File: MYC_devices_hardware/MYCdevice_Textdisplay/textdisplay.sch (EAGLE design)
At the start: 25 parts, among them IC1 MEGA8-P, IC2 78L05, Q1 20MHz, Q2 BC307, X1 8-15V, X2 1503_09, X3 1503_09

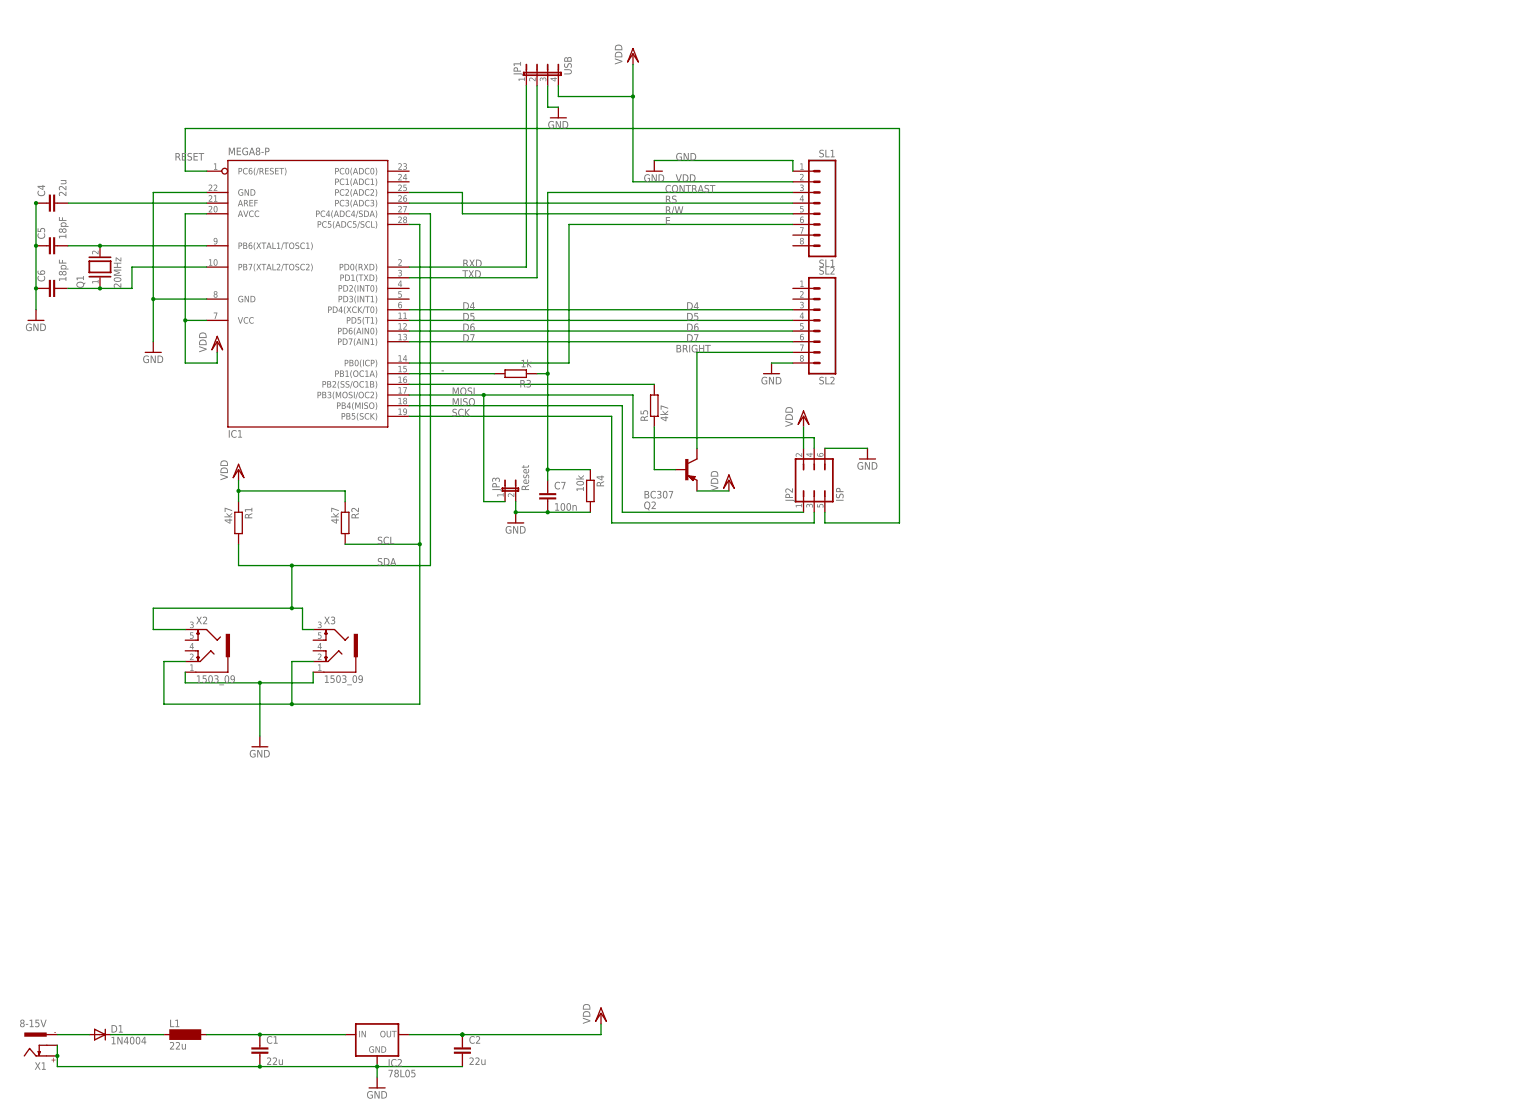
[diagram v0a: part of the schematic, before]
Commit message: now with includefiles, new board
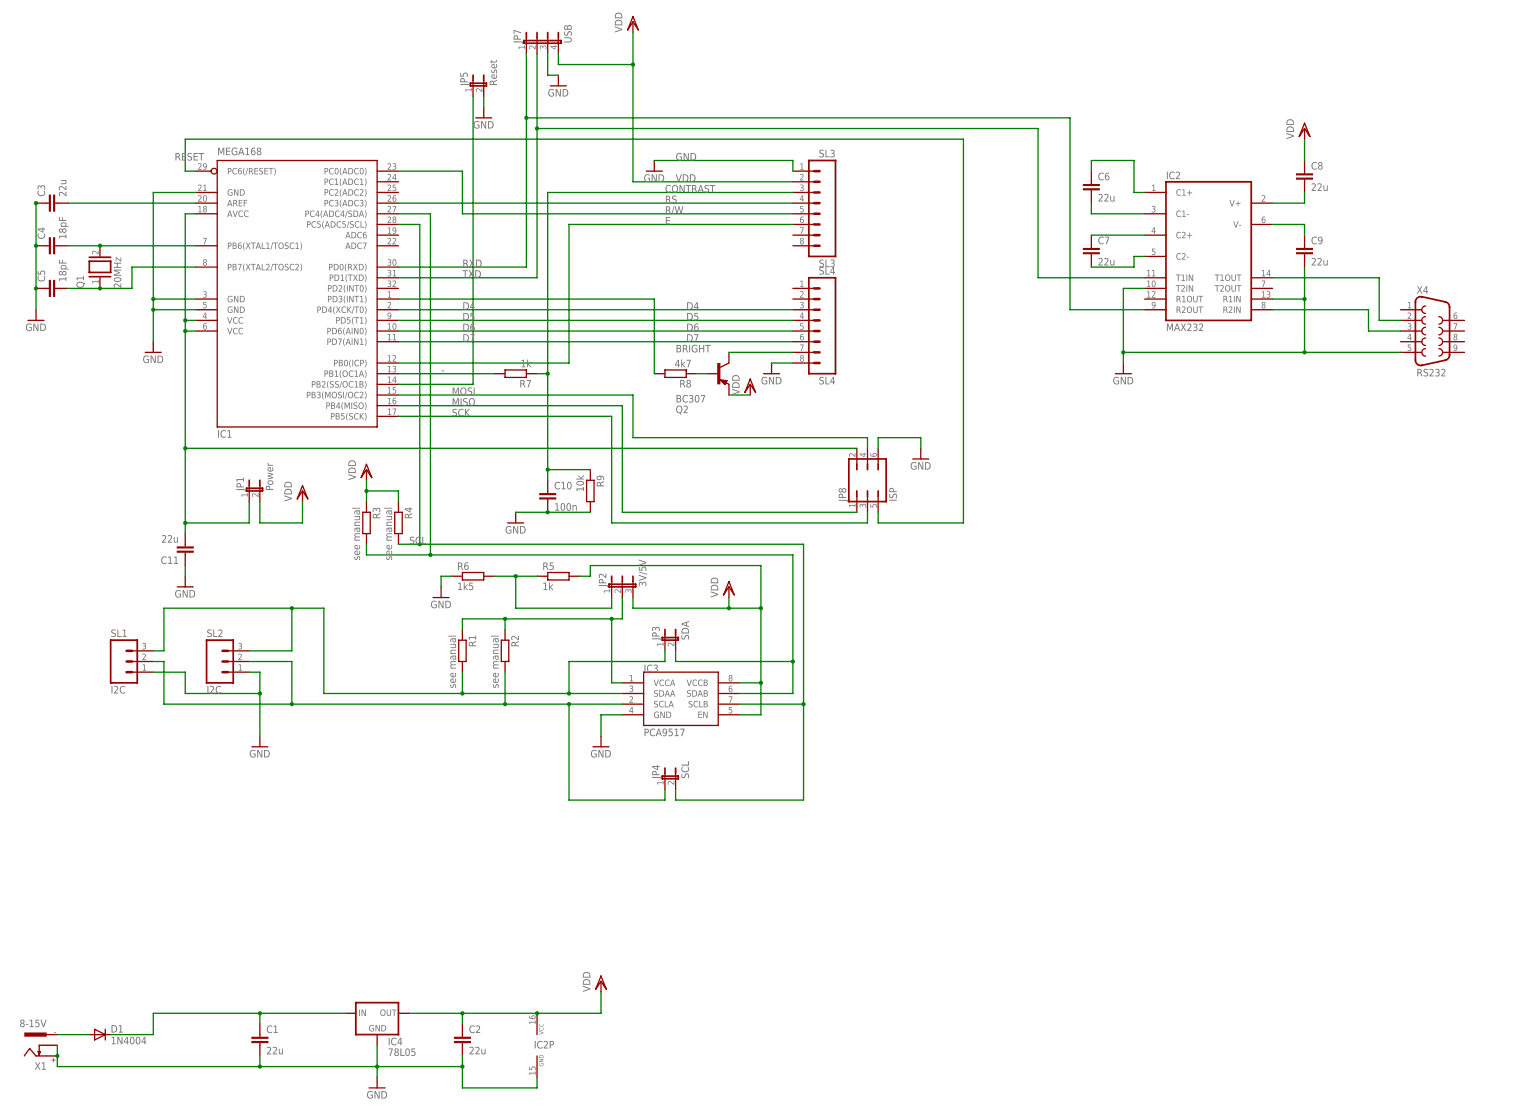
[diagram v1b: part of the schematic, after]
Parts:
- removed L1: 22u, inductor-neosid:MS85
- removed X2, X3: 1503_09, con-lumberg:1503_09
- added C10: 100n, resistor:C-EU050-025X075
- added C11, C3, C8, C9: 22u, resistor:C-EUC1206
- added IC3: PCA9517, PCA9517:PCA9517
- added IC4: 78L05, v-reg:78LXX
- added JP4: SCL, jumper:JP1E
- added JP5: Reset, jumper:JP1E
- added JP7: USB, jumper:JP4E
- added JP8: ISP, jumper:JP3Q
- added R6: 1k5, resistor:R-EU_R1206
- added R7: 1k, resistor:R-EU_R1206
- added R8: 4k7, resistor:R-EU_R1206
- added R9: 10k, resistor:R-EU_R1206
- added SL3: SL3, con-amp-quick:M08
- added SL4: SL4, con-amp-quick:M08
- added X4: RS232, con-subd:F09H
- C4: value 22u -> 18pF; device resistor:C-EUC1206 -> resistor:C-EU025-025X050
- C6: value 18pF -> 22u; device resistor:C-EU025-025X050 -> resistor:C-EUC1206
- C7: value 100n -> 22u; device resistor:C-EU050-025X075 -> resistor:C-EUC1206
- IC1: value MEGA8-P -> MEGA168; device atmel:MEGA8-P -> atmel:MEGA8-AI
- IC2: value 78L05 -> MAX232; device v-reg:78LXX -> maxim:MAX232
- JP1: value USB -> Power; device jumper:JP4E -> jumper:JP1E
- JP2: value ISP -> 3V/5V; device jumper:JP3Q -> jumper:JP2E
- JP3: value Reset -> SDA
- R1, R2: value 4k7 -> see manual; device resistor:R-EU_0207/2V -> resistor:R-EU_R1206
- R3: value 1k -> see manual; device resistor:R-EU_0207/2V -> resistor:R-EU_R1206
- R4: value 10k -> see manual; device resistor:R-EU_0207/2V -> resistor:R-EU_R1206
- R5: value 4k7 -> 1k; device resistor:R-EU_0207/2V -> resistor:R-EU_R1206
- SL1: value SL1 -> I2C; device con-amp-quick:M08 -> con-amp-quick:M03
- SL2: value SL2 -> I2C; device con-amp-quick:M08 -> con-amp-quick:M03
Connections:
- new net N$11: C9.1, IC2G$1.V-
- new net N$12: C8.2, IC2G$1.V+
- new net N$13: C6.1, IC2G$1.C1+
- new net N$14: IC2G$1.R2IN, X4.3
- new net N$15: IC2G$1.T1OUT, X4.2
- new net N$16: IC1.PB2(SS/OC1B), JP5.1
- new net N$24: IC3.VCCA, JP2.2, R1.1, R2.1
- new net N$3: IC3.SDAA, JP3.1, R1.2, SL1.3, SL2.3
- new net N$5: IC3.SCLA, JP4.1, R2.2, SL1.2, SL2.2
- new net N$6: C11.2, IC1.AVCC, IC1.VCC@1, IC1.VCC@2, JP1.1, JP8.2
- new net N$7: C6.2, IC2G$1.C1-
- new net N$8: C7.1, IC2G$1.C2+
- new net N$9: C7.2, IC2G$1.C2-
- net -: now also R7.2; no longer R3.2
- net BRIGHT: now also SL4.7; no longer SL2.7
- net CONTRAST: now also C10.1, R7.1, R9.1, SL3.3; no longer C7.1, R3.1, R4.1, SL1.3
- net D4: now also SL4.3; no longer SL2.3
- net D5: now also SL4.4; no longer SL2.4
- net D6: now also SL4.5; no longer SL2.5
- net D7: now also SL4.6; no longer SL2.6
- net E: now also SL3.6; no longer SL1.6
- net GND: now also C10.2, C11.1, C3.1, C9.2, IC1.GND@2, IC2G$1.R1IN, IC2G$1.T2IN, IC2P.GND, IC3.GND, IC4.GND, JP5.2, JP7.3, JP8.6, R6.1, R9.2, SL2.1, SL3.1, SL4.8, X4.5; no longer C6.1, C7.2, IC2.GND, JP1.3, JP2.6, JP3.2, R4.2, SL2.8, X2.1, X3.1
- net MISO: now also JP8.1; no longer JP2.1
- net MOSI: now also JP8.4; no longer JP2.4, JP3.1
- net N$1: now also JP2.1, R5.1, R6.2; no longer D1.C, L1.1
- net N$18: now also D1.C, IC4.IN; no longer IC2.IN, L1.2
- net N$19: now also C4.2; no longer C5.2
- net N$2: now also IC1.PD3(INT1), R8.2; no longer IC1.PB2(SS/OC1B), R5.2
- net N$35: now also C3.2; no longer C4.2
- net N$37: now also C5.2; no longer C6.2
- net N$4: now also R8.1; no longer R5.1
- net R/W: now also IC1.PC0(ADC0), SL3.5; no longer IC1.PC2(ADC2), SL1.5
- net RESET: now also JP8.5; no longer JP2.5
- net RS: now also SL3.4; no longer SL1.4
- net RXD: now also IC2G$1.R2OUT, JP7.1; no longer JP1.1
- net SCK: now also JP8.3; no longer JP2.3
- net SCL: now also IC3.SCLB, JP4.2, R4.2; no longer R2.2, X2.2, X3.2
- net SDA: now also IC3.SDAB, JP3.2, R3.2; no longer R1.2, X2.3, X3.3
- net TXD: now also IC2G$1.T1IN, JP7.2; no longer JP1.2
- net VDD: now also C8.1, IC2P.VCC, IC3.EN, IC3.VCCB, IC4.OUT, JP1.2, JP2.3, JP7.4, R3.1, R4.1, R5.2, SL3.2; no longer IC1.AVCC, IC1.VCC@1, IC2.OUT, JP1.4, JP2.2, R1.1, R2.1, SL1.2
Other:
- moved on the sheet: C1, C2, C4, C5, C6, C7, JP3, Q2, R1, R2, R3, R4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
